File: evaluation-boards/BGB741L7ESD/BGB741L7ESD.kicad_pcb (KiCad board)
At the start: 4 copper layers, 42 x 40 mm, 22 parts, among them J1 CONN_01X01, J2 CONN_01X01, J3 CONN_01X03, J4 CONN_COAXIAL, J5 CONN_COAXIAL, J6 CONN_COAXIAL, J7 CONN_COAXIAL, U1 BGB741L7ESD

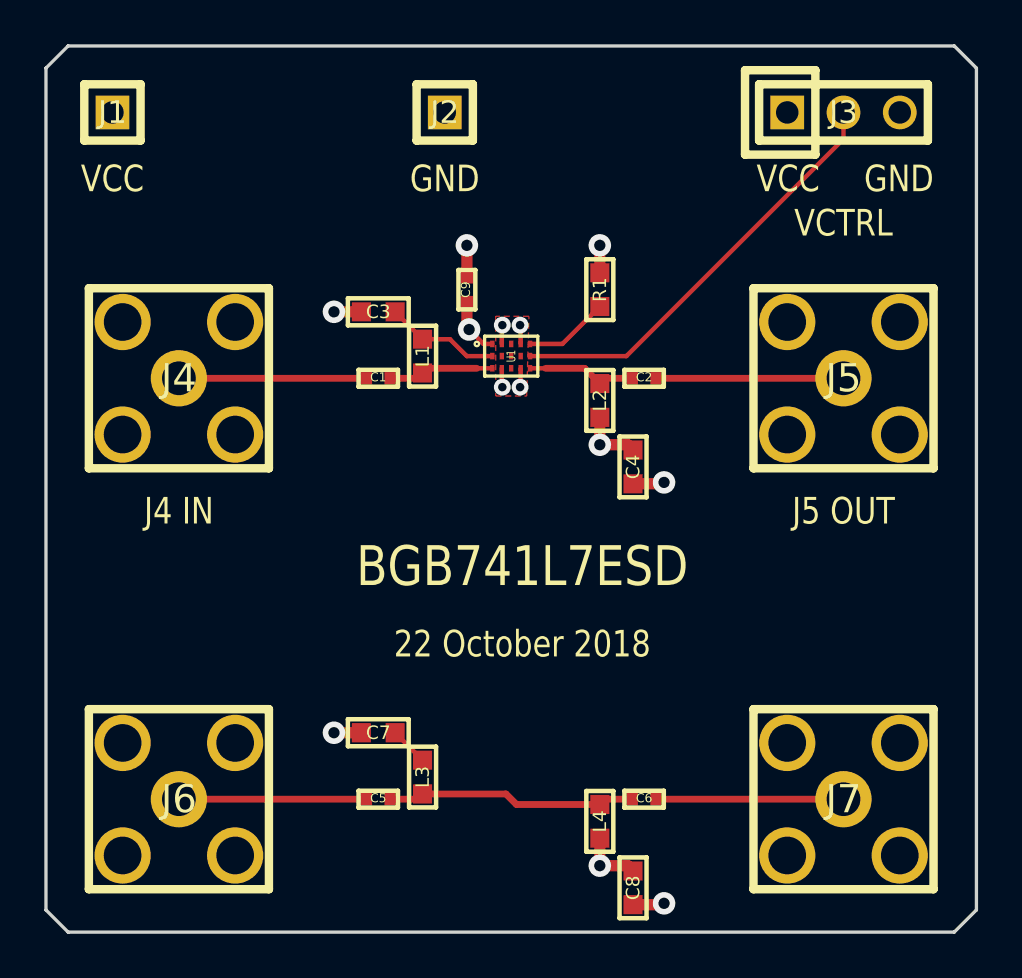
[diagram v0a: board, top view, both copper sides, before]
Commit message: BGB741L7ESD: update with PCB edge SMA connectors
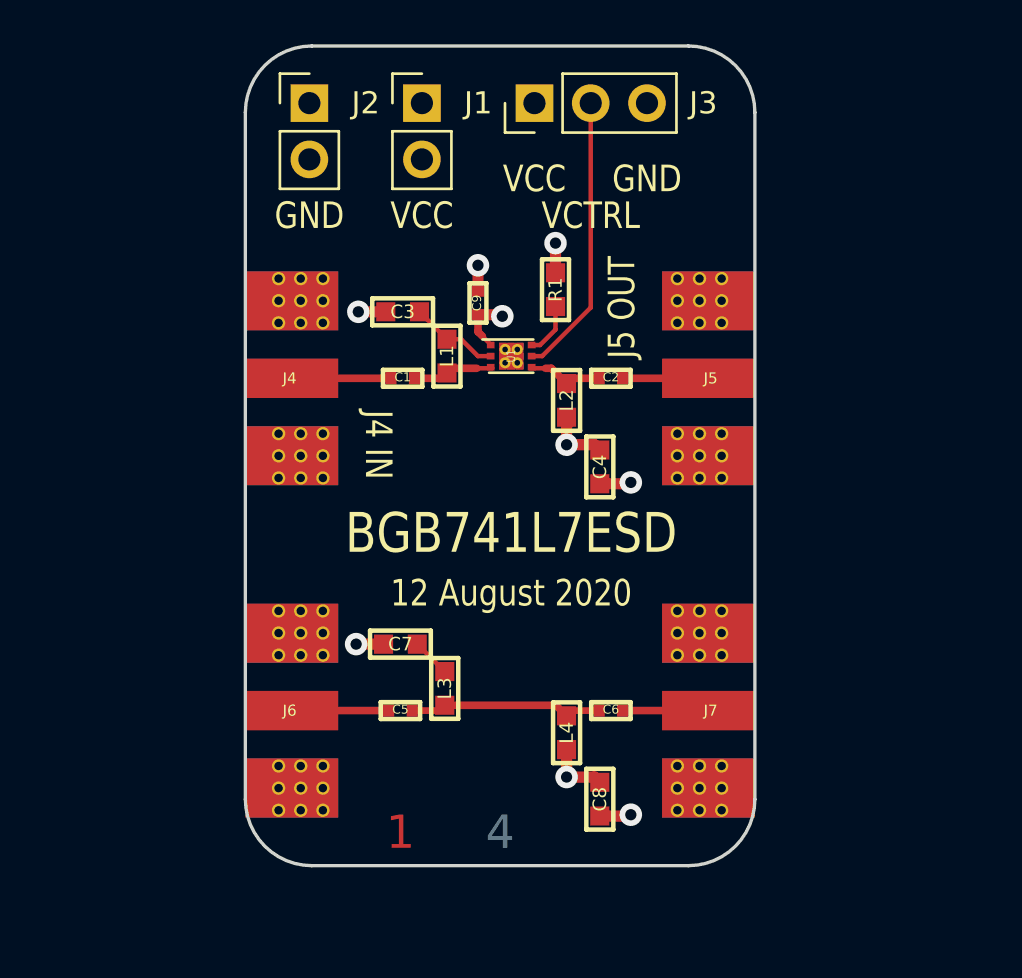
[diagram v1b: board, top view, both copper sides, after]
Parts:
- J1, J2: value CONN_01X01 -> Conn_01x02; footprint gsg-modules:HEADER-1x1 -> Connector_PinHeader_2.54mm:PinHeader_1x02_P2.54mm_Vertical
- J3: footprint gsg-modules:HEADER-1x3 -> Connector_PinHeader_2.54mm:PinHeader_1x03_P2.54mm_Vertical
- J4, J5, J6, J7: footprint gsg-modules:SMA-VERTICAL -> gsg-modules:SMA-73251-2120
- moved J1 14.0 mm to (141.0, 68.6)
- moved J3 14.0 mm to (146.1, 68.6), turned to 90 degrees
- moved J2 6.12 mm to (135.9, 68.6)
- moved J7 5.66 mm to (156.0, 96.0), turned to 180 degrees
- moved J6 5.00 mm to (133.0, 96.0)
- moved C6 4.27 mm to (149.5, 96.0)
- moved C8 4.27 mm to (149.0, 100.0)
- moved L4 4.27 mm to (147.5, 97.0)
- moved C5 4.12 mm to (140.0, 96.0)
- moved C7 4.12 mm to (140.0, 93.0)
- moved L3 4.12 mm to (142.0, 95.0)
- moved J5 4.00 mm to (156.0, 81.0), turned to 180 degrees
- moved J4 3.00 mm to (133.0, 81.0)
- moved R1 2.00 mm to (147.0, 77.0)
- moved C2 1.50 mm to (149.5, 81.0)
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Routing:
- net Net-(J3-Pad2): track 19.4 -> 12.8 mm
- net Net-(C6-Pad1): track 8.47 -> 3.87 mm
- net Net-(C2-Pad1): track 8.47 -> 3.87 mm
- net Net-(C5-Pad2): track 8.47 -> 4.37 mm
- net Net-(C1-Pad2): track 8.47 -> 4.47 mm
- net GND: track 10.2 -> 6.49 mm, vias 9 -> 5
- net Net-(C5-Pad1): track 11.3 -> 8.83 mm
- net Net-(C2-Pad2): track 5.00 -> 3.50 mm
- net Net-(R1-Pad2): track 3.85 -> 2.40 mm
- net Net-(C3-Pad2): track 5.22 -> 4.04 mm
- net Net-(C1-Pad1): track 4.80 -> 3.70 mm
- removed copper zone on F.Cu, net GND
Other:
- board size 42 x 40 mm -> 23 x 37 mm
- board text added: "1"
- board text added: "12 August 2020"
- board text added: "2"
- board text added: "3"
- board text added: "4"
- board text removed: "22 October 2018"
